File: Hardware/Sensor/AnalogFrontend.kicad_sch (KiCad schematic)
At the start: 41 parts, among them J3 RF_Shield_One_Piece, J4 Conn_Coaxial, J5 Conn_01x03_Male, J6 Conn_01x03_Male, Q1 Q_PMOS_GDS, Q2 Q_PMOS_GDS, Q3 Q_NMOS_GDS, Q4 Q_NMOS_GDS, U3 LMC662, U4 LM358

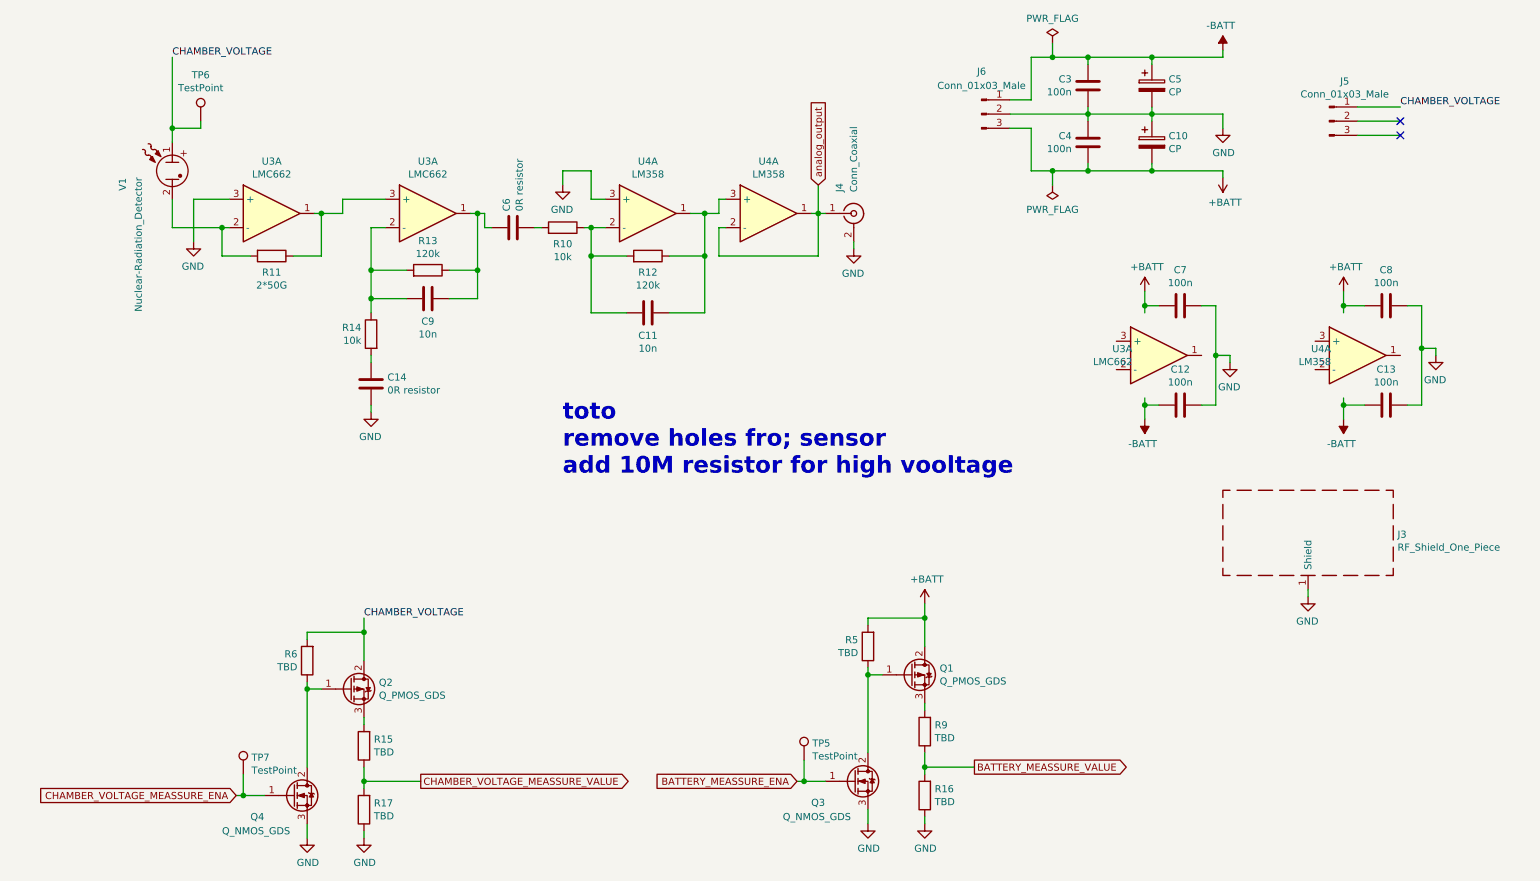
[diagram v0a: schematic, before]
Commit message: this is what was send for pcb production
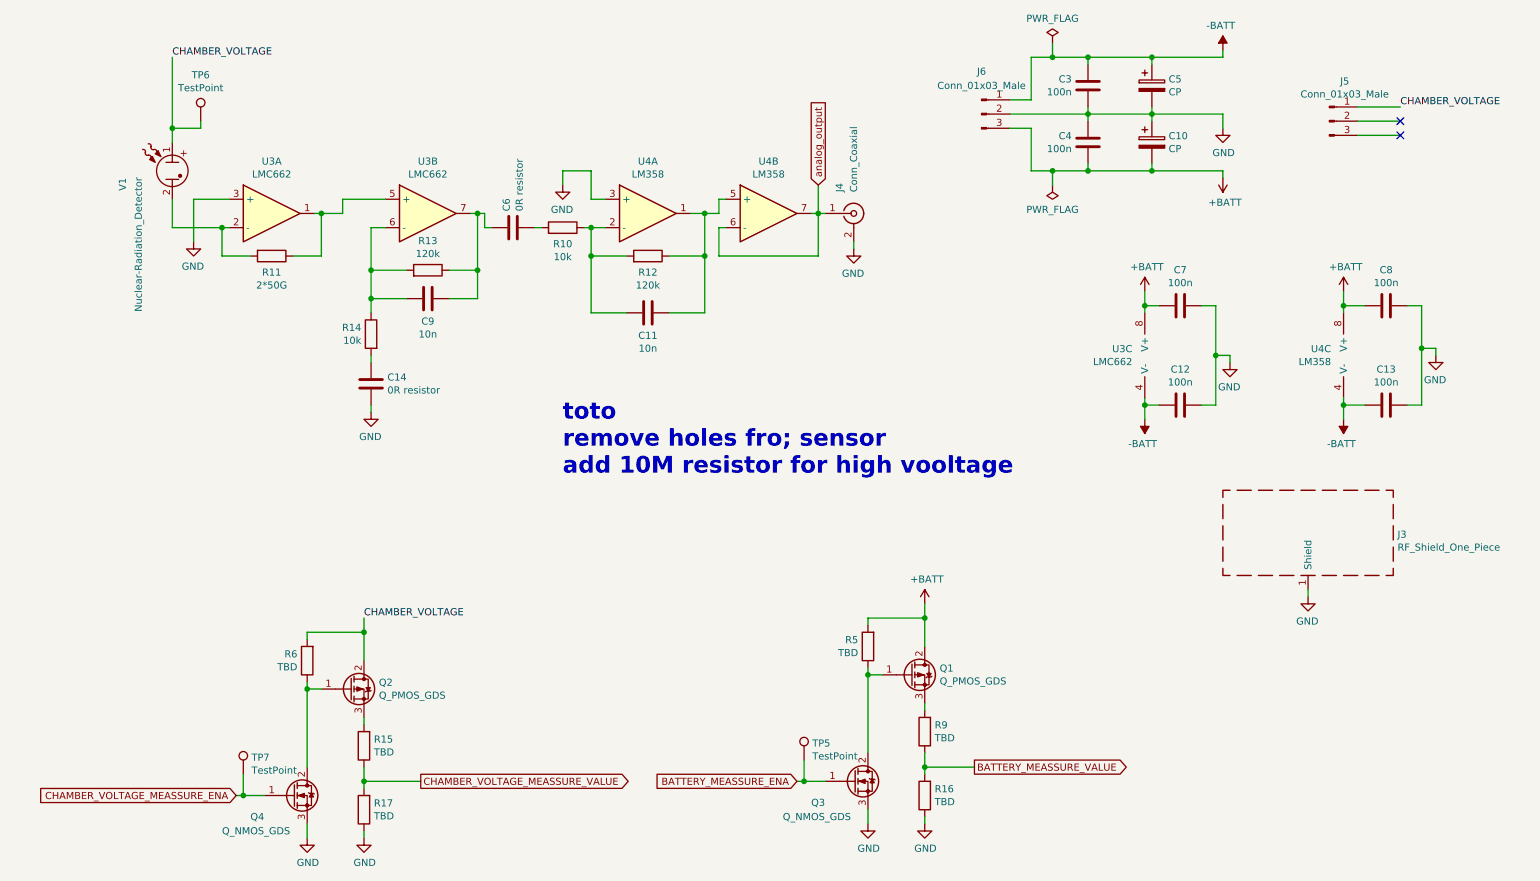
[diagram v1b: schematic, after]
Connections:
- net +BATT: now also U3.8 (V+), U4.8 (V+)
- net -BATT: now also U3.4 (V-), U4.4 (V-)
- net analog_output: now also U4.6 (-), U4.7; no longer U4.1, U4.2 (-)
- net at R11.1, U3.1: now also U3.5 (+); no longer U3.3 (+)
- net at C6.1, C9.2, R13.1: now also U3.7; no longer U3.1
- net at C9.1, R13.2, R14.1: now also U3.6 (-); no longer U3.2 (-)
- net at C11.2, R12.1, U4.1: now also U4.5 (+); no longer U4.3 (+)
